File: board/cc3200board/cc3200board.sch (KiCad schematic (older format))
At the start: 38 parts, among them U1 CC3200, U2 N25Q128A13ESE40E, X1 32.768kH, X2 ABM3B-40.000MHZ-10-1-U-T

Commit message: Rev 1.0 of CC3200board
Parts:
- U1: value CC3200 -> CC3200R1M2RGCR
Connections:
- net GND: now also E1.3 (GND); no longer C9.1, E1.1, L1.2
- net DCDC_ANA: now reaches C10.1, C11.1, C13.1, C14.1, L2.1, U1.25 (LDO_IN2), U1.36 (LDO_IN1), U1.48 (VDD_ANA1)
- net DC_PA: now reaches C15.1, C16.1, C17.1, U1.33 (VDD_PA_IN), U1.42 (DCDC_PA_OUT)
- net DCDC_DIG: now reaches C18.1, C19.1, C20.1, L8.1, U1.56 (VDD_DIG2), U1.9 (VDD_DIG1)
- new net FEED: C9.1, E1.1, L1.2
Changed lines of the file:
@@
 P 4000 4450
 F 0 "U1" H 2650 7250 45  0000 C CNN
-F 1 "CC3200" H 5050 1950 45  0000 C CNN
+F 1 "CC3200R1M2RGCR" H 5050 1950 45  0000 C CNN
 F 2 "VQFN64" H 4200 4050 35  0000 C CIN
 F 3 "~" H 4350 4200 60  0000 C CNN
@@
 $EndComp
 $Comp
-L GND #PWR019
-U 1 1 5452E1D2
-P 9875 5975
-F 0 "#PWR019" H 9875 5975 30  0001 C CNN
-F 1 "GND" H 9875 5905 30  0001 C CNN
-F 2 "" H 9875 5975 60  0000 C CNN
-F 3 "" H 9875 5975 60  0000 C CNN
-	1    9875 5975
-	1    0    0    -1
-$EndComp
-$Comp
 L GND #PWR020
 U 1 1 5452E53F
@@
 Connection ~ 1450 3300
 Wire Wire Line
-	700  3550 700  3700
+	700  3550 700  3925
 Wire Wire Line
 	2250 3750 2350 3750
@@
 Connection ~ 1450 3150
 Wire Wire Line
-	1450 3700 1450 3550
-Wire Wire Line
-	700  3700 1450 3700
+	1450 3550 1450 3900
 Wire Wire Line
 	1075 3700 1075 3925
 Wire Wire Line
-	1250 3550 1250 3700
+	1250 3700 1250 3550
 Connection ~ 1250 3700
 Wire Wire Line
@@
 Wire Wire Line
 	9100 5650 9875 5650
-Wire Wire Line
-	9875 5600 9875 5975
 Connection ~ 9875 5650
 Wire Wire Line
-	10550 5150 10550 5425
+	10550 5075 10550 5425
 Wire Wire Line
 	10475 5150 10550 5150
@@
 Text Label 9575 1200 0    60   ~ 0
 nRESET
+Text Label 700  2650 0    60   ~ 0
+DCDC_ANA
+Text Label 1100 5400 0    60   ~ 0
+SGND
+$Comp
+L GND #PWR028
+U 1 1 547963D9
+P 1450 3900
+F 0 "#PWR028" H 1450 3900 30  0001 C CNN
+F 1 "GND" H 1450 3830 30  0001 C CNN
+F 2 "" H 1450 3900 60  0000 C CNN
+F 3 "" H 1450 3900 60  0000 C CNN
+	1    1450 3900
+	1    0    0    -1
+$EndComp
+$Comp
+L GND #PWR029
+U 1 1 5479640A
+P 700 3925
+F 0 "#PWR029" H 700 3925 30  0001 C CNN
+F 1 "GND" H 700 3855 30  0001 C CNN
+F 2 "" H 700 3925 60  0000 C CNN
+F 3 "" H 700 3925 60  0000 C CNN
+	1    700  3925
+	1    0    0    -1
+$EndComp
+Wire Wire Line
+	900  3700 1250 3700
+Text Label 1925 5200 0    60   ~ 0
+DCDC_DIG
+Text Label 1500 4200 0    60   ~ 0
+DC_PA
+Wire Wire Line
+	10550 5075 10375 5075
+Connection ~ 10550 5150
+Wire Wire Line
+	9875 5650 9875 5600
+Text Label 9325 5650 0    60   ~ 0
+FEED
 $EndSCHEMATC

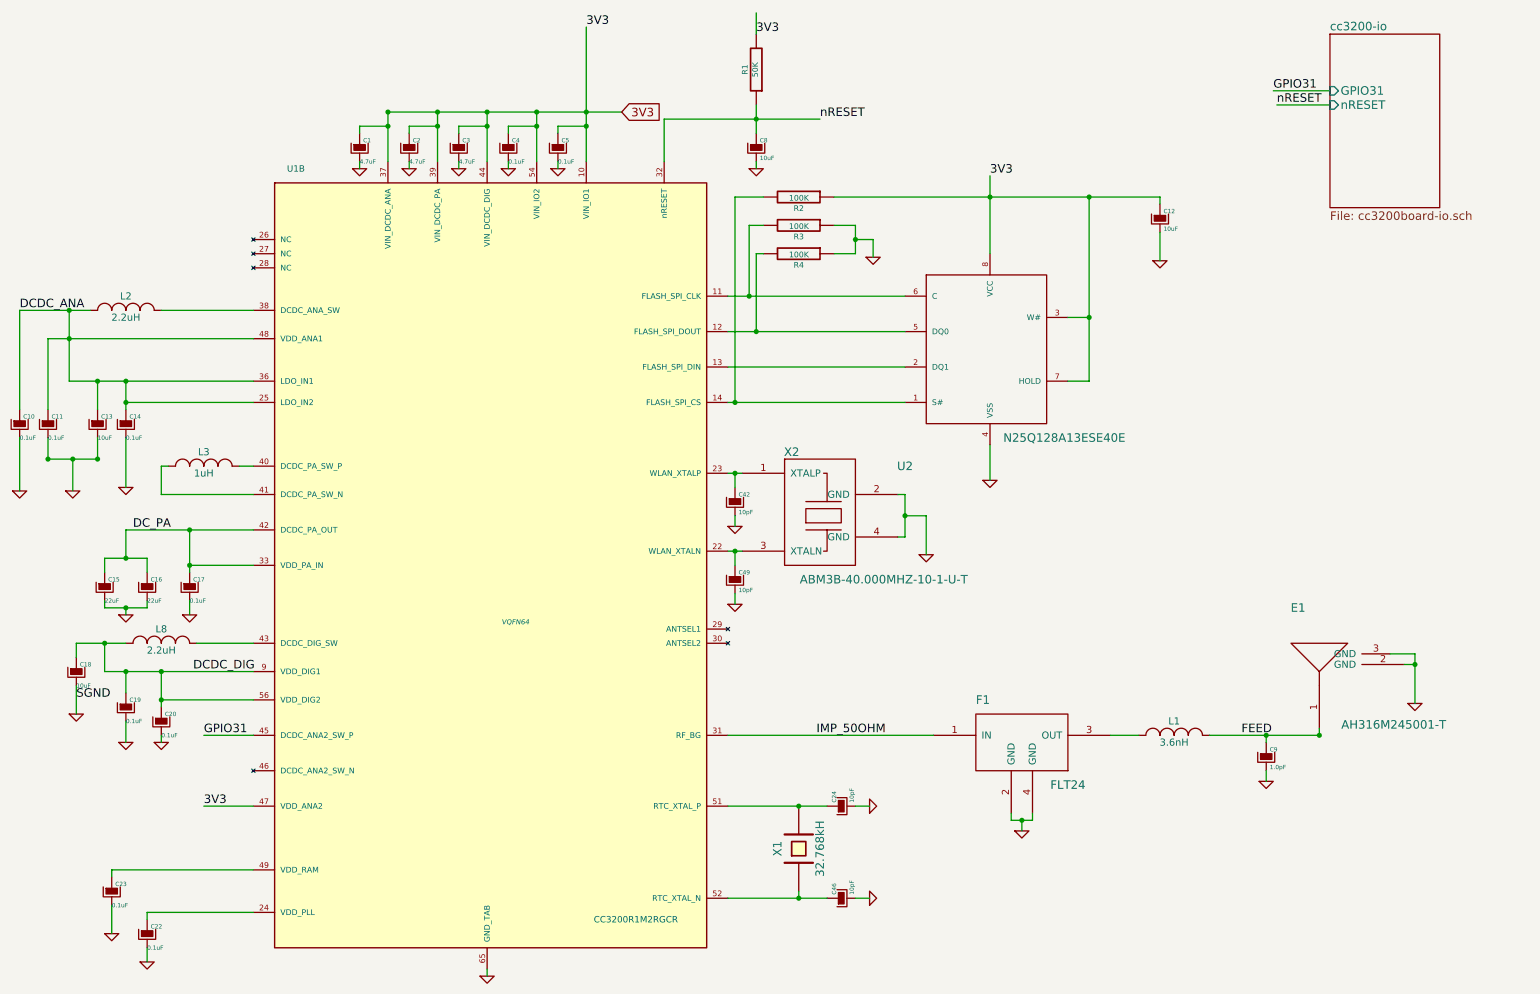
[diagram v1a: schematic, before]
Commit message: Fixed error in GND plane on L4
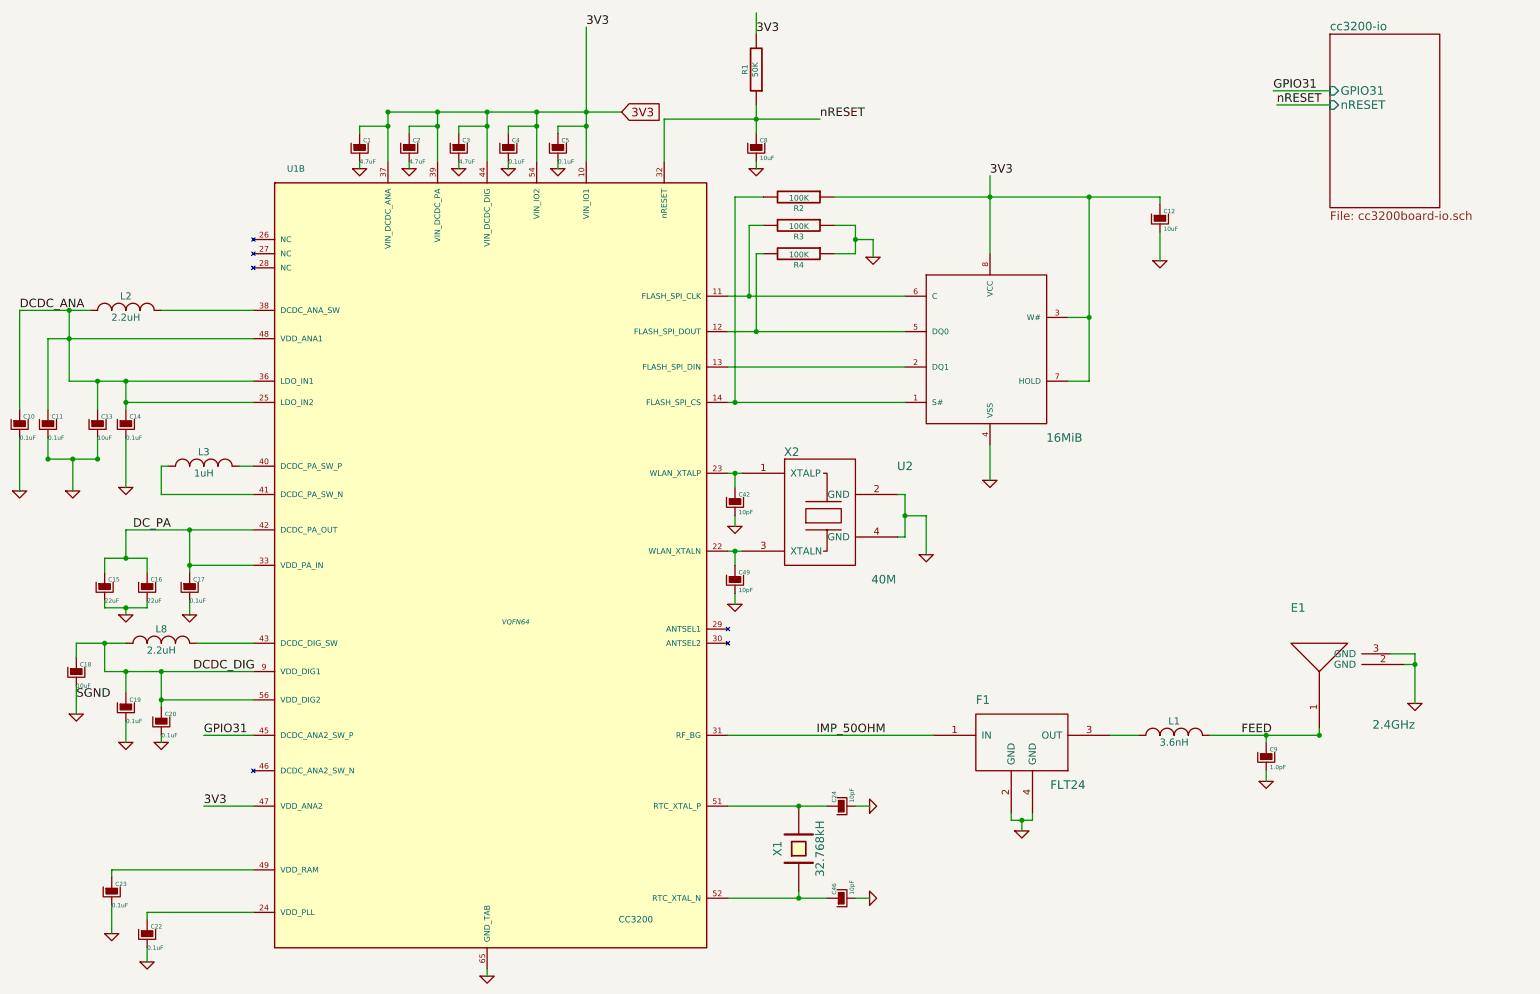
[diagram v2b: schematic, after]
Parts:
- E1: value AH316M245001-T -> 2.4GHz; PartNum (none) -> AH316M245001-T
- U1: value CC3200R1M2RGCR -> CC3200; PartNum (none) -> CC3200R1M2RGCR
- U2: value N25Q128A13ESE40E -> 16MiB; PartNum (none) -> N25Q128A13ESE40E
- X2: value ABM3B-40.000MHZ-10-1-U-T -> 40M; PartNumber (none) -> ABM3B-40.000MHZ-10-1-U-T
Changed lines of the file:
@@
 P 4000 4450
 F 0 "U1" H 2650 7250 45  0000 C CNN
-F 1 "CC3200R1M2RGCR" H 5050 1950 45  0000 C CNN
+F 1 "CC3200" H 5050 1950 45  0000 C CNN
 F 2 "VQFN64" H 4200 4050 35  0000 C CIN
 F 3 "~" H 4350 4200 60  0000 C CNN
+F 4 "CC3200R1M2RGCR" H 4000 4450 60  0001 C CNN "PartNum"
 	2    4000 4450
 	1    0    0    -1
@@
 P 7550 2950
 F 0 "U2" H 6950 2150 60  0000 C CNN
-F 1 "N25Q128A13ESE40E" H 8075 2350 60  0000 C CNN
+F 1 "16MiB" H 8075 2350 60  0000 C CNN
 F 2 "" H 7350 2700 60  0000 C CNN
 F 3 "~" H 7350 2700 60  0000 C CNN
+F 4 "N25Q128A13ESE40E" H 7550 2950 60  0001 C CNN "PartNum"
 	1    7550 2950
 	1    0    0    -1
@@
 P 6450 4100
 F 0 "X2" H 6150 4550 60  0000 C CNN
-F 1 "ABM3B-40.000MHZ-10-1-U-T" H 6800 3650 60  0000 C CNN
+F 1 "40M" H 6800 3650 60  0000 C CNN
 F 2 "" H 7250 3550 60  0001 C CNN
 F 3 "" H 7250 3550 60  0000 C CNN
+F 4 "ABM3B-40.000MHZ-10-1-U-T" H 6450 4100 60  0001 C CNN "PartNumber"
 	1    6450 4100
 	1    0    0    -1
@@
 P 9875 5300
 F 0 "E1" H 9725 5850 60  0000 C CNN
-F 1 "AH316M245001-T" H 10400 5025 60  0000 C CNN
+F 1 "2.4GHz" H 10400 5025 60  0000 C CNN
 F 2 "" H 9875 5300 60  0001 C CNN
 F 3 "" H 9875 5300 60  0000 C CNN
+F 4 "AH316M245001-T" H 9875 5300 60  0001 C CNN "PartNum"
 	1    9875 5300
 	1    0    0    -1
 $EndComp
 $Comp
-L GND #PWR020
+L GND #PWR019
 U 1 1 5452E53F
 P 10550 5425
-F 0 "#PWR020" H 10550 5425 30  0001 C CNN
+F 0 "#PWR019" H 10550 5425 30  0001 C CNN
 F 1 "GND" H 10550 5355 30  0001 C CNN
 F 2 "" H 10550 5425 60  0000 C CNN
@@
 $EndComp
 $Comp
-L GND #PWR021
+L GND #PWR020
 U 1 1 5452EA23
 P 9500 5975
-F 0 "#PWR021" H 9500 5975 30  0001 C CNN
+F 0 "#PWR020" H 9500 5975 30  0001 C CNN
 F 1 "GND" H 9500 5905 30  0001 C CNN
 F 2 "" H 9500 5975 60  0000 C CNN
@@
 $EndComp
 $Comp
-L GND #PWR022
+L GND #PWR021
 U 1 1 5452EA43
 P 8750 2300
-F 0 "#PWR022" H 8750 2300 30  0001 C CNN
+F 0 "#PWR021" H 8750 2300 30  0001 C CNN
 F 1 "GND" H 8750 2230 30  0001 C CNN
 F 2 "" H 8750 2300 60  0000 C CNN
@@
 $EndComp
 $Comp
-L GND #PWR023
+L GND #PWR022
 U 1 1 5452EB03
 P 5750 4175
-F 0 "#PWR023" H 5750 4175 30  0001 C CNN
+F 0 "#PWR022" H 5750 4175 30  0001 C CNN
 F 1 "GND" H 5750 4105 30  0001 C CNN
 F 2 "" H 5750 4175 60  0000 C CNN
@@
 $EndComp
 $Comp
-L GND #PWR024
+L GND #PWR023
 U 1 1 5452EBEE
 P 5750 4725
-F 0 "#PWR024" H 5750 4725 30  0001 C CNN
+F 0 "#PWR023" H 5750 4725 30  0001 C CNN
 F 1 "GND" H 5750 4655 30  0001 C CNN
 F 2 "" H 5750 4725 60  0000 C CNN
@@
 $EndComp
 $Comp
-L GND #PWR025
+L GND #PWR024
 U 1 1 5452ECD1
 P 7550 3850
-F 0 "#PWR025" H 7550 3850 30  0001 C CNN
+F 0 "#PWR024" H 7550 3850 30  0001 C CNN
 F 1 "GND" H 7550 3780 30  0001 C CNN
 F 2 "" H 7550 3850 60  0000 C CNN
@@
 $EndComp
 $Comp
-L GND #PWR026
+L GND #PWR025
 U 1 1 5452EE39
 P 7100 4375
-F 0 "#PWR026" H 7100 4375 30  0001 C CNN
+F 0 "#PWR025" H 7100 4375 30  0001 C CNN
 F 1 "GND" H 7100 4305 30  0001 C CNN
 F 2 "" H 7100 4375 60  0000 C CNN
@@
 $EndComp
 $Comp
-L GND #PWR027
+L GND #PWR026
 U 1 1 5452EFCF
 P 6725 2275
-F 0 "#PWR027" H 6725 2275 30  0001 C CNN
+F 0 "#PWR026" H 6725 2275 30  0001 C CNN
 F 1 "GND" H 6725 2205 30  0001 C CNN
 F 2 "" H 6725 2275 60  0000 C CNN
@@
 SGND
 $Comp
-L GND #PWR028
+L GND #PWR027
 U 1 1 547963D9
 P 1450 3900
-F 0 "#PWR028" H 1450 3900 30  0001 C CNN
+F 0 "#PWR027" H 1450 3900 30  0001 C CNN
 F 1 "GND" H 1450 3830 30  0001 C CNN
 F 2 "" H 1450 3900 60  0000 C CNN
@@
 $EndComp
 $Comp
-L GND #PWR029
+L GND #PWR028
 U 1 1 5479640A
 P 700 3925
-F 0 "#PWR029" H 700 3925 30  0001 C CNN
+F 0 "#PWR028" H 700 3925 30  0001 C CNN
 F 1 "GND" H 700 3855 30  0001 C CNN
 F 2 "" H 700 3925 60  0000 C CNN
